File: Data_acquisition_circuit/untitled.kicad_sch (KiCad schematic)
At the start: 8 parts, among them U2 MAX3232

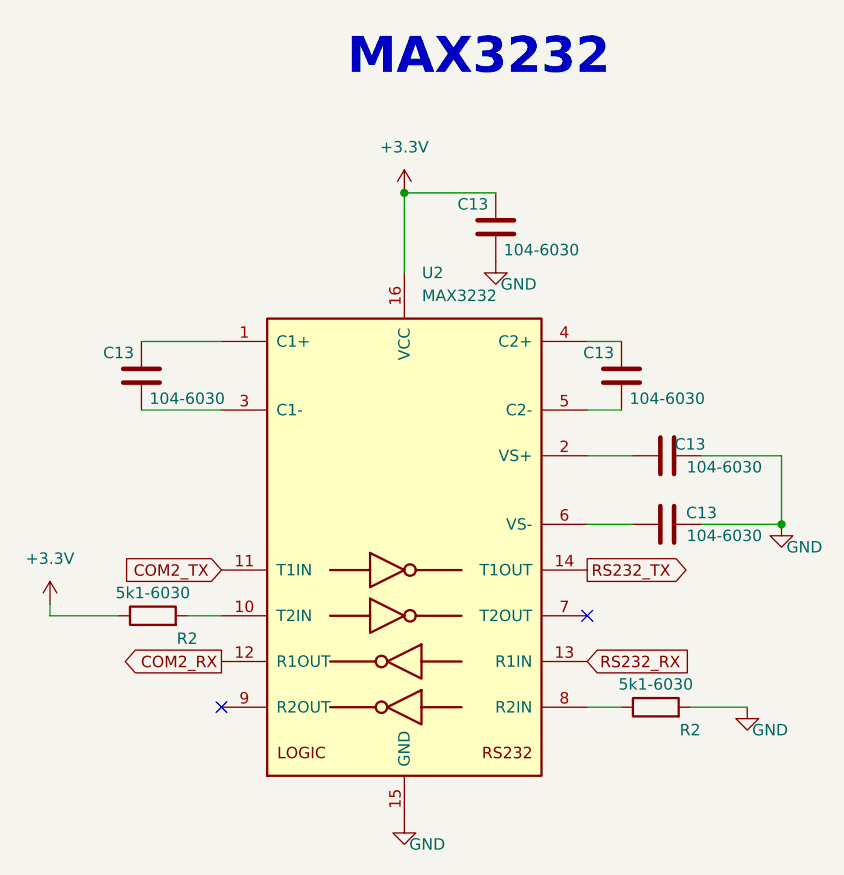
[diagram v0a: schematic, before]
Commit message: covert 0603 to 0805
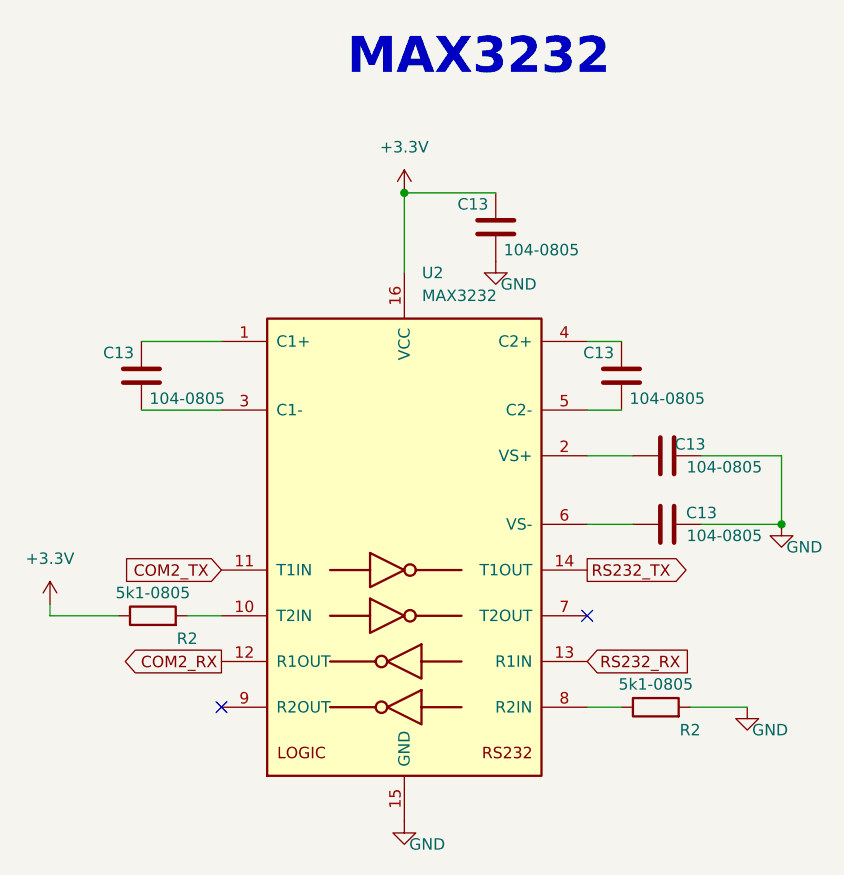
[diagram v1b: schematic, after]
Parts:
- C13: value 104-6030 -> 104-0805
- R2: value 5k1-6030 -> 5k1-0805
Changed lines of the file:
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@@
       (effects (font (size 1.27 1.27)))
     )
-    (property "Value" "5k1-6030" (at 160.02 111.76 90)
+    (property "Value" "5k1-0805" (at 160.02 111.76 90)
       (effects (font (size 1.27 1.27)))
     )
@@
       (effects (font (size 1.27 1.27)))
     )
-    (property "Value" "104-6030" (at 107.95 80.01 0)
+    (property "Value" "104-0805" (at 107.95 80.01 0)
       (effects (font (size 1.27 1.27)))
     )
@@
       (effects (font (size 1.27 1.27)))
     )
-    (property "Value" "104-6030" (at 167.64 95.25 90)
+    (property "Value" "104-0805" (at 167.64 95.25 90)
       (effects (font (size 1.27 1.27)))
     )
@@
       (effects (font (size 1.27 1.27)))
     )
-    (property "Value" "104-6030" (at 147.32 63.5 0)
+    (property "Value" "104-0805" (at 147.32 63.5 0)
       (effects (font (size 1.27 1.27)))
     )
@@
       (effects (font (size 1.27 1.27)))
     )
-    (property "Value" "104-6030" (at 167.64 87.63 90)
+    (property "Value" "104-0805" (at 167.64 87.63 90)
       (effects (font (size 1.27 1.27)))
     )
@@
       (effects (font (size 1.27 1.27)))
     )
-    (property "Value" "104-6030" (at 161.29 80.01 0)
+    (property "Value" "104-0805" (at 161.29 80.01 0)
       (effects (font (size 1.27 1.27)))
     )
@@
       (effects (font (size 1.27 1.27)))
     )
-    (property "Value" "5k1-6030" (at 104.14 101.6 90)
-      (effects (font (size 1.27 1.27)))
-    )
+    (property "Value" "5k1-0805" (at 104.14 101.6 90)
+      (effects (font (size 1.27 1.27)))
+    )
